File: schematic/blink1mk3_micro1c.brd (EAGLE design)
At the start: 15.2 x 9.6 mm, 15 parts, among them U1 EFM32HG309F64G, X1 USBPCB2

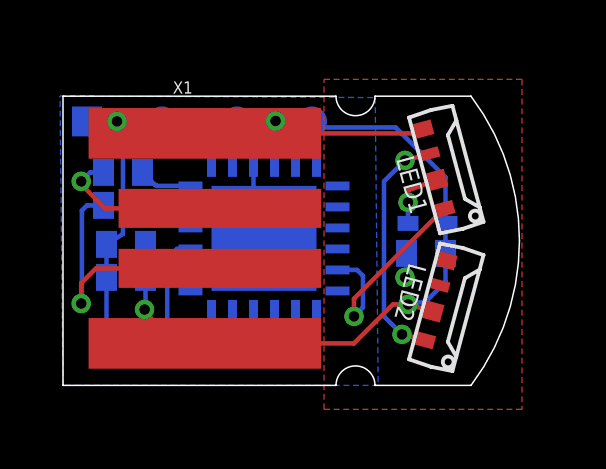
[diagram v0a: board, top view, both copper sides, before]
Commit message: fix EFM32HG309 pad spacing issue. omg what a slog
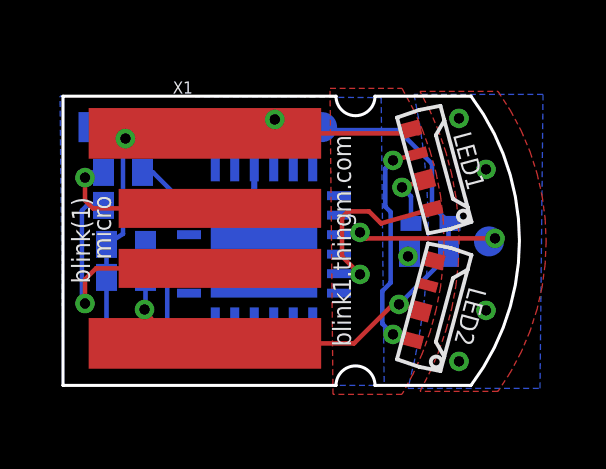
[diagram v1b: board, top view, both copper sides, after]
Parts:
- added TOUCH: TPTP10R, testpad:TP10R
- D1: value (none) -> 1N4148
- moved LED1 0.40 mm to (12.4, 7.20)
- moved LED2 0.40 mm to (12.4, 2.60)
- moved 5V 0.39 mm to (8.64, 8.61)
- moved D 0.35 mm to (6.10, 8.61)
- moved C 0.32 mm to (3.56, 8.61)
- moved G 0.29 mm to (1.02, 8.61)
- moved U1 0.20 mm to (6.70, 4.70)
- moved C4 0.10 mm to (12.2, 4.40)
- moved D1 0.10 mm to (12.2, 5.40)
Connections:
- net CAP0A: now also TOUCH.TP
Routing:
- net CAP0A: track 0.00 -> 5.54 mm, vias 0 -> 6
- net +5V: track 24.5 -> 23.2 mm
- net DI: track 7.22 -> 6.16 mm
- added copper zone on layer 1, net CAP0A
- added copper zone on layer 16, net CAP0A
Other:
- board text added: "blink(1)"
- board text added: "blink1.thingm.com"
- board text added: "blink1mk2_micro1cB"
- board text added: "micro"

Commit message: added blink1mk3-test5
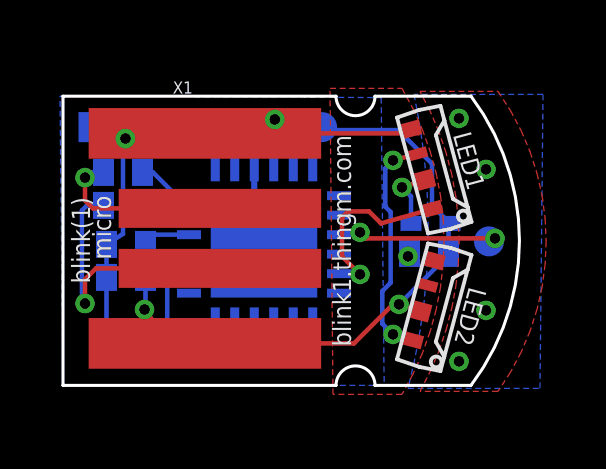
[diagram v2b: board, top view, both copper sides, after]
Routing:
- net +3V3: track 0.00 -> 1.58 mm
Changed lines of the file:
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@@
 <grid distance="0.1" unitdist="mm" unit="mm" style="lines" multiple="1" display="no" altdistance="1" altunitdist="mm" altunit="mm"/>
 <layers>
-<layer number="1" name="Top" color="4" fill="1" visible="no" active="yes"/>
+<layer number="1" name="Top" color="4" fill="1" visible="yes" active="yes"/>
 <layer number="2" name="Route2" color="1" fill="3" visible="no" active="no"/>
 <layer number="3" name="Route3" color="4" fill="3" visible="no" active="no"/>
@@
 <vertex x="0" y="0"/>
 </polygon>
+<wire x1="4.2" y1="5.025" x2="3.075" y2="5.025" width="0.1524" layer="16"/>
+<wire x1="3.075" y1="5.025" x2="2.75" y2="4.7" width="0.1524" layer="16"/>
+<wire x1="7.025" y1="7.2" x2="9.2" y2="5.675" width="0" layer="19" extent="16-16"/>
+<wire x1="4.2" y1="5.025" x2="7.025" y2="7.2" width="0" layer="19" extent="16-16"/>
+<wire x1="4.2" y1="3.075" x2="4.2" y2="5.025" width="0" layer="19" extent="16-16"/>
+<wire x1="5.075" y1="2.2" x2="4.2" y2="3.075" width="0" layer="19" extent="16-16"/>
+<wire x1="7.025" y1="2.2" x2="5.075" y2="2.2" width="0" layer="19" extent="16-16"/>
 </signal>
 <signal name="VDEC">
